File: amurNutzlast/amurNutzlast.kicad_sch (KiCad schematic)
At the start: 6 parts, among them J1 Conn_01x08, J3 Conn_01x02, J4 Conn_01x08, J5 Conn_01x07, J7 Conn_01x07, J8 Conn_01x20

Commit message: layout ftdi placement
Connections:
- net GND: no longer J3.1 (Pin_1)
- net fpga/FTDI_CTS: now also J7.4 (Pin_4); no longer J7.7 (Pin_7)
- net fpga/FTDI_DCD: now also J7.1 (Pin_1); no longer J7.4 (Pin_4)
- net fpga/FTDI_DSR: now also J7.2 (Pin_2); no longer J7.5 (Pin_5)
- net fpga/FTDI_DTR: now also J7.3 (Pin_3); no longer J7.6 (Pin_6)
- net fpga/FTDI_RTS: now also J7.5 (Pin_5); no longer J7.1 (Pin_1)
- net fpga/FTDI_RX: now also J7.7 (Pin_7); no longer J7.3 (Pin_3)
- net fpga/FTDI_TX: now also J7.6 (Pin_6); no longer J7.2 (Pin_2)
- new net +5V: J3.1 (Pin_1)
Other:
- note added: "jumper to supply input power to the FPGA"
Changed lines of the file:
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@@
   (junction (at 144.78 68.58) (diameter 0) (color 0 0 0 0)
   )
+  (wire (pts (xy 111.76 160.02) (xy 137.16 160.02))
+    (stroke (width 0) (type default))
+  )
   (wire (pts (xy 154.94 139.7) (xy 132.08 139.7))
     (stroke (width 0) (type default))
   )
+  (wire (pts (xy 68.58 20.32) (xy 68.58 27.94))
+    (stroke (width 0) (type default))
+  )
   (wire (pts (xy 129.54 137.16) (xy 154.94 137.16))
     (stroke (width 0) (type default))
   )
+  (wire (pts (xy 111.76 157.48) (xy 134.62 157.48))
+    (stroke (width 0) (type default))
+  )
   (wire (pts (xy 129.54 152.4) (xy 129.54 137.16))
     (stroke (width 0) (type default))
@@
     (stroke (width 0) (type default))
   )
+  (wire (pts (xy 111.76 152.4) (xy 129.54 152.4))
+    (stroke (width 0) (type default))
+  )
   (wire (pts (xy 111.76 132.08) (xy 114.3 132.08))
     (stroke (width 0) (type default))
@@
     (stroke (width 0) (type default))
   )
-  (wire (pts (xy 132.08 154.94) (xy 111.76 154.94))
+  (wire (pts (xy 111.76 162.56) (xy 139.7 162.56))
     (stroke (width 0) (type default))
   )
@@
     (stroke (width 0) (type default))
   )
+  (wire (pts (xy 185.42 68.58) (xy 200.66 68.58))
+    (stroke (width 0) (type default))
+  )
+  (wire (pts (xy 55.88 27.94) (xy 68.58 27.94))
+    (stroke (width 0) (type default))
+  )
+  (wire (pts (xy 111.76 96.52) (xy 114.3 96.52))
+    (stroke (width 0) (type default))
+  )
+  (wire (pts (xy 147.32 81.28) (xy 152.4 81.28))
+    (stroke (width 0) (type default))
+  )
+  (wire (pts (xy 111.76 63.5) (xy 139.7 63.5))
+    (stroke (width 0) (type default))
+  )
+  (wire (pts (xy 111.76 129.54) (xy 114.3 129.54))
+    (stroke (width 0) (type default))
+  )
+  (wire (pts (xy 144.78 167.64) (xy 144.78 152.4))
+    (stroke (width 0) (type default))
+  )
+  (wire (pts (xy 111.76 121.92) (xy 114.3 121.92))
+    (stroke (width 0) (type default))
+  )
+  (wire (pts (xy 185.42 137.16) (xy 200.66 137.16))
+    (stroke (width 0) (type default))
+  )
+  (wire (pts (xy 111.76 109.22) (xy 114.3 109.22))
+    (stroke (width 0) (type default))
+  )
+  (wire (pts (xy 185.42 66.04) (xy 200.66 66.04))
+    (stroke (width 0) (type default))
+  )
+  (wire (pts (xy 111.76 124.46) (xy 114.3 124.46))
+    (stroke (width 0) (type default))
+  )
+  (wire (pts (xy 154.94 76.2) (xy 154.94 81.28))
+    (stroke (width 0) (type default))
+  )
+  (wire (pts (xy 149.86 33.02) (xy 149.86 71.12))
+    (stroke (width 0) (type default))
+  )
+  (wire (pts (xy 185.42 73.66) (xy 193.04 73.66))
+    (stroke (width 0) (type default))
+  )
+  (wire (pts (xy 111.76 111.76) (xy 114.3 111.76))
+    (stroke (width 0) (type default))
+  )
+  (wire (pts (xy 154.94 149.86) (xy 142.24 149.86))
+    (stroke (width 0) (type default))
+  )
+  (wire (pts (xy 111.76 71.12) (xy 149.86 71.12))
+    (stroke (width 0) (type default))
+  )
+  (wire (pts (xy 111.76 60.96) (xy 157.48 60.96))
+    (stroke (width 0) (type default))
+  )
+  (wire (pts (xy 111.76 101.6) (xy 114.3 101.6))
+    (stroke (width 0) (type default))
+  )
   (wire (pts (xy 111.76 167.64) (xy 144.78 167.64))
     (stroke (width 0) (type default))
   )
-  (wire (pts (xy 185.42 68.58) (xy 200.66 68.58))
-    (stroke (width 0) (type default))
-  )
-  (wire (pts (xy 60.96 27.94) (xy 55.88 27.94))
-    (stroke (width 0) (type default))
-  )
-  (wire (pts (xy 111.76 96.52) (xy 114.3 96.52))
-    (stroke (width 0) (type default))
-  )
-  (wire (pts (xy 147.32 81.28) (xy 152.4 81.28))
-    (stroke (width 0) (type default))
-  )
-  (wire (pts (xy 111.76 63.5) (xy 139.7 63.5))
-    (stroke (width 0) (type default))
-  )
-  (wire (pts (xy 111.76 129.54) (xy 114.3 129.54))
-    (stroke (width 0) (type default))
-  )
-  (wire (pts (xy 111.76 152.4) (xy 129.54 152.4))
-    (stroke (width 0) (type default))
-  )
-  (wire (pts (xy 144.78 167.64) (xy 144.78 152.4))
-    (stroke (width 0) (type default))
-  )
-  (wire (pts (xy 111.76 162.56) (xy 139.7 162.56))
-    (stroke (width 0) (type default))
-  )
-  (wire (pts (xy 111.76 121.92) (xy 114.3 121.92))
-    (stroke (width 0) (type default))
-  )
-  (wire (pts (xy 185.42 137.16) (xy 200.66 137.16))
-    (stroke (width 0) (type default))
-  )
-  (wire (pts (xy 111.76 109.22) (xy 114.3 109.22))
-    (stroke (width 0) (type default))
-  )
-  (wire (pts (xy 185.42 66.04) (xy 200.66 66.04))
-    (stroke (width 0) (type default))
-  )
-  (wire (pts (xy 111.76 124.46) (xy 114.3 124.46))
-    (stroke (width 0) (type default))
-  )
-  (wire (pts (xy 154.94 76.2) (xy 154.94 81.28))
-    (stroke (width 0) (type default))
-  )
-  (wire (pts (xy 149.86 33.02) (xy 149.86 71.12))
-    (stroke (width 0) (type default))
-  )
-  (wire (pts (xy 185.42 73.66) (xy 193.04 73.66))
-    (stroke (width 0) (type default))
-  )
-  (wire (pts (xy 111.76 111.76) (xy 114.3 111.76))
-    (stroke (width 0) (type default))
-  )
-  (wire (pts (xy 154.94 149.86) (xy 142.24 149.86))
-    (stroke (width 0) (type default))
-  )
-  (wire (pts (xy 111.76 71.12) (xy 149.86 71.12))
-    (stroke (width 0) (type default))
-  )
-  (wire (pts (xy 111.76 60.96) (xy 157.48 60.96))
-    (stroke (width 0) (type default))
-  )
-  (wire (pts (xy 111.76 101.6) (xy 114.3 101.6))
-    (stroke (width 0) (type default))
-  )
   (wire (pts (xy 147.32 78.74) (xy 147.32 81.28))
     (stroke (width 0) (type default))
@@
     (stroke (width 0) (type default))
   )
-  (wire (pts (xy 137.16 160.02) (xy 111.76 160.02))
-    (stroke (width 0) (type default))
-  )
   (wire (pts (xy 111.76 68.58) (xy 144.78 68.58))
     (stroke (width 0) (type default))
@@
     (stroke (width 0) (type default))
   )
-  (wire (pts (xy 111.76 157.48) (xy 134.62 157.48))
-    (stroke (width 0) (type default))
-  )
   (wire (pts (xy 185.42 71.12) (xy 200.66 71.12))
     (stroke (width 0) (type default))
@@
     (stroke (width 0) (type default))
   )
-  (wire (pts (xy 142.24 165.1) (xy 111.76 165.1))
+  (wire (pts (xy 111.76 165.1) (xy 142.24 165.1))
     (stroke (width 0) (type default))
   )
@@
     (stroke (width 0) (type default))
   )
-  (wire (pts (xy 60.96 27.94) (xy 60.96 35.56))
-    (stroke (width 0) (type default))
-  )
   (wire (pts (xy 137.16 144.78) (xy 137.16 160.02))
     (stroke (width 0) (type default))
   )
+  (wire (pts (xy 111.76 154.94) (xy 132.08 154.94))
+    (stroke (width 0) (type default))
+  )
   (wire (pts (xy 111.76 58.42) (xy 157.48 58.42))
     (stroke (width 0) (type default))
@@
   (wire (pts (xy 152.4 81.28) (xy 152.4 73.66))
     (stroke (width 0) (type default))
+  )
+  (text "jumper to supply input\npower to the FPGA" (at 73.66 22.86 0)
+    (effects (font (size 1.27 1.27)) (justify left bottom))
   )
   (label "ICE_CDONE" (at 116.84 60.96 0) (fields_autoplaced)
@@
     )
   )
-  (symbol (lib_id "power:GND") (at 60.96 35.56 0) (unit 1)
-    (in_bom yes) (on_board yes) (dnp no) (fields_autoplaced)
-    (property "Reference" "#PWR087" (at 60.96 41.91 0)
-      (effects (font (size 1.27 1.27)) hide)
-    )
-    (property "Value" "GND" (at 60.96 40.64 0)
-      (effects (font (size 1.27 1.27)))
-    )
-    (property "Footprint" "" (at 60.96 35.56 0)
-      (effects (font (size 1.27 1.27)) hide)
-    )
-    (property "Datasheet" "" (at 60.96 35.56 0)
+  (symbol (lib_id "power:+5V") (at 68.58 20.32 0) (unit 1)
+    (in_bom yes) (on_board yes) (dnp no) (fields_autoplaced)
+    (property "Reference" "#PWR087" (at 68.58 24.13 0)
+      (effects (font (size 1.27 1.27)) hide)
+    )
+    (property "Value" "+5V" (at 68.58 15.24 0)
+      (effects (font (size 1.27 1.27)))
+    )
+    (property "Footprint" "" (at 68.58 20.32 0)
+      (effects (font (size 1.27 1.27)) hide)
+    )
+    (property "Datasheet" "" (at 68.58 20.32 0)
       (effects (font (size 1.27 1.27)) hide)
     )
@@
       (effects (font (size 1.27 1.27)) (justify right))
     )
-    (pin "FTDI_RTS" input (at 111.76 152.4 0)
-      (effects (font (size 1.27 1.27)) (justify right))
-    )
-    (pin "FTDI_TX" input (at 111.76 154.94 0)
-      (effects (font (size 1.27 1.27)) (justify right))
-    )
-    (pin "FTDI_DCD" input (at 111.76 160.02 0)
-      (effects (font (size 1.27 1.27)) (justify right))
-    )
-    (pin "FTDI_DSR" input (at 111.76 162.56 0)
-      (effects (font (size 1.27 1.27)) (justify right))
-    )
-    (pin "FTDI_DTR" input (at 111.76 165.1 0)
-      (effects (font (size 1.27 1.27)) (justify right))
-    )
-    (pin "FTDI_CTS" input (at 111.76 167.64 0)
-      (effects (font (size 1.27 1.27)) (justify right))
-    )
-    (pin "FTDI_RX" output (at 111.76 157.48 0)
-      (effects (font (size 1.27 1.27)) (justify right))
-    )
+    (pin "FTDI_RTS" input (at 111.76 162.56 0)
+      (effects (font (size 1.27 1.27)) (justify right))
+    )
+    (pin "FTDI_TX" input (at 111.76 165.1 0)
+      (effects (font (size 1.27 1.27)) (justify right))
+    )
+    (pin "FTDI_DCD" input (at 111.76 152.4 0)
+      (effects (font (size 1.27 1.27)) (justify right))
+    )
+    (pin "FTDI_DSR" input (at 111.76 154.94 0)
+      (effects (font (size 1.27 1.27)) (justify right))
+    )
+    (pin "FTDI_DTR" input (at 111.76 157.48 0)
+      (effects (font (size 1.27 1.27)) (justify right))
+    )
+    (pin "FTDI_CTS" input (at 111.76 160.02 0)
+      (effects (font (size 1.27 1.27)) (justify right))
+    )
+    (pin "FTDI_RX" output (at 111.76 167.64 0)
+      (effects (font (size 1.27 1.27)) (justify right))
+    )

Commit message: ftdi layout continuation
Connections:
- net ftdi/CTS: now also J5.4 (Pin_4); no longer J5.1 (Pin_1)
- net ftdi/DCD: now also J5.1 (Pin_1); no longer J5.4 (Pin_4)
- net ftdi/DSR: now also J5.2 (Pin_2); no longer J5.3 (Pin_3)
- net ftdi/DTR: now also J5.3 (Pin_3); no longer J5.2 (Pin_2)
- net ftdi/RTS: now also J5.5 (Pin_5); no longer J5.7 (Pin_7)
- net ftdi/RX: now also J5.7 (Pin_7); no longer J5.5 (Pin_5)

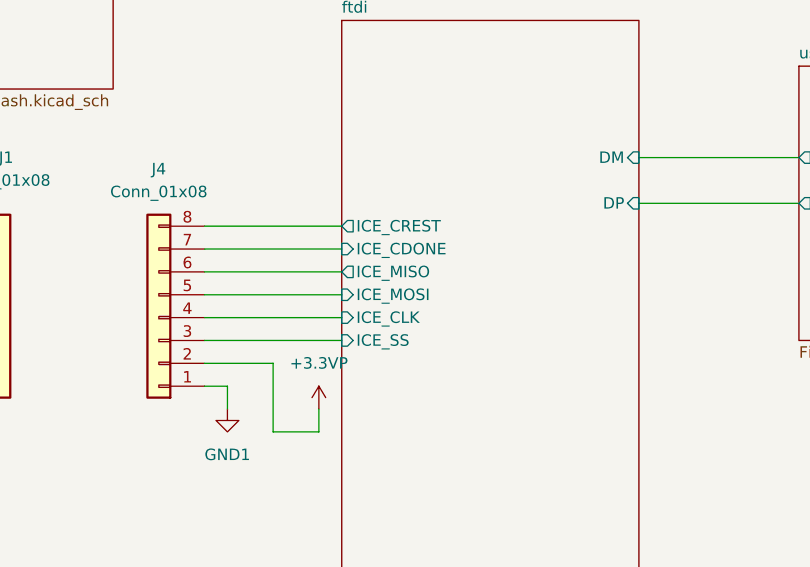
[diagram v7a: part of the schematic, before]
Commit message: ftdi layout finish
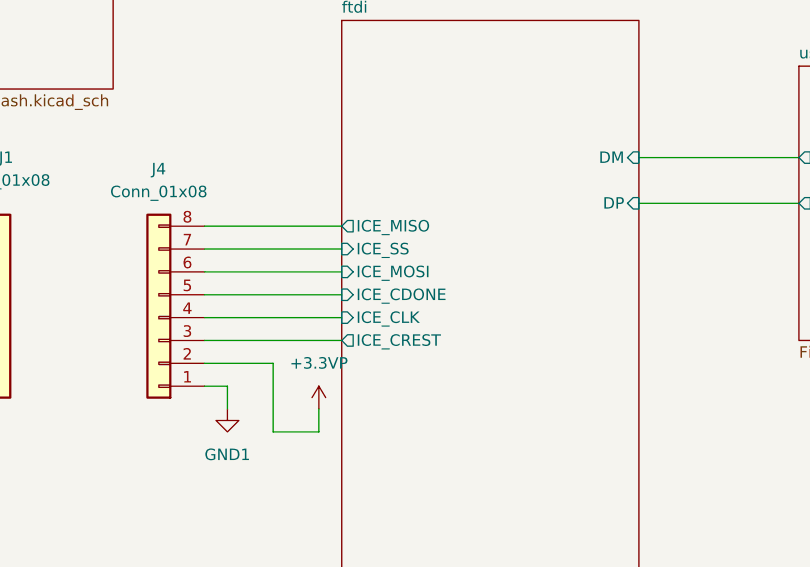
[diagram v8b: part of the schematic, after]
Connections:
- net ftdi/ICE_CDONE: now also J4.5 (Pin_5); no longer J4.7 (Pin_7)
- net ftdi/ICE_CREST: now also J4.3 (Pin_3); no longer J4.8 (Pin_8)
- net ftdi/ICE_MISO: now also J4.8 (Pin_8); no longer J4.6 (Pin_6)
- net ftdi/ICE_MOSI: now also J4.6 (Pin_6); no longer J4.5 (Pin_5)
- net ftdi/ICE_SS: now also J4.7 (Pin_7); no longer J4.3 (Pin_3)
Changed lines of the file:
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@@
+    (stroke (width 0) (type default))
+  )
+  (wire (pts (xy 185.42 58.42) (xy 200.66 58.42))
     (stroke (width 0) (type default))
   )
@@
     (stroke (width 0) (type default))
   )
+  (wire (pts (xy 185.42 63.5) (xy 200.66 63.5))
+    (stroke (width 0) (type default))
+  )
   (wire (pts (xy 111.76 121.92) (xy 114.3 121.92))
     (stroke (width 0) (type default))
@@
     (stroke (width 0) (type default))
   )
+  (wire (pts (xy 111.76 124.46) (xy 114.3 124.46))
+    (stroke (width 0) (type default))
+  )
   (wire (pts (xy 185.42 66.04) (xy 200.66 66.04))
     (stroke (width 0) (type default))
   )
-  (wire (pts (xy 111.76 124.46) (xy 114.3 124.46))
-    (stroke (width 0) (type default))
-  )
   (wire (pts (xy 154.94 76.2) (xy 154.94 81.28))
     (stroke (width 0) (type default))
@@
     (stroke (width 0) (type default))
   )
-  (wire (pts (xy 185.42 63.5) (xy 200.66 63.5))
-    (stroke (width 0) (type default))
-  )
   (wire (pts (xy 60.96 20.32) (xy 60.96 25.4))
     (stroke (width 0) (type default))
@@
     (stroke (width 0) (type default))
   )
+  (wire (pts (xy 185.42 60.96) (xy 200.66 60.96))
+    (stroke (width 0) (type default))
+  )
   (wire (pts (xy 53.34 86.36) (xy 71.12 86.36))
     (stroke (width 0) (type default))
@@
     (stroke (width 0) (type default))
   )
-  (wire (pts (xy 185.42 60.96) (xy 200.66 60.96))
-    (stroke (width 0) (type default))
-  )
   (wire (pts (xy 139.7 147.32) (xy 154.94 147.32))
     (stroke (width 0) (type default))
   )
+  (wire (pts (xy 111.76 142.24) (xy 114.3 142.24))
+    (stroke (width 0) (type default))
+  )
   (wire (pts (xy 185.42 71.12) (xy 200.66 71.12))
     (stroke (width 0) (type default))
   )
-  (wire (pts (xy 111.76 142.24) (xy 114.3 142.24))
-    (stroke (width 0) (type default))
-  )
   (wire (pts (xy 111.76 134.62) (xy 114.3 134.62))
     (stroke (width 0) (type default))
@@
   )
   (wire (pts (xy 154.94 144.78) (xy 137.16 144.78))
-    (stroke (width 0) (type default))
-  )
-  (wire (pts (xy 185.42 58.42) (xy 200.66 58.42))
     (stroke (width 0) (type default))
   )
@@
       (effects (font (size 1.27 1.27)) (justify left))
     )
-    (pin "ICE_MISO" output (at 200.66 63.5 180)
-      (effects (font (size 1.27 1.27)) (justify left))
-    )
-    (pin "ICE_CDONE" input (at 200.66 60.96 180)
-      (effects (font (size 1.27 1.27)) (justify left))
-    )
-    (pin "ICE_MOSI" input (at 200.66 66.04 180)
-      (effects (font (size 1.27 1.27)) (justify left))
-    )
-    (pin "ICE_SS" input (at 200.66 71.12 180)
+    (pin "ICE_MISO" output (at 200.66 58.42 180)
+      (effects (font (size 1.27 1.27)) (justify left))
+    )
+    (pin "ICE_CDONE" input (at 200.66 66.04 180)
+      (effects (font (size 1.27 1.27)) (justify left))
+    )
+    (pin "ICE_MOSI" input (at 200.66 63.5 180)
+      (effects (font (size 1.27 1.27)) (justify left))
+    )
+    (pin "ICE_SS" input (at 200.66 60.96 180)
       (effects (font (size 1.27 1.27)) (justify left))
     )
@@
       (effects (font (size 1.27 1.27)) (justify left))
     )
-    (pin "ICE_CREST" output (at 200.66 58.42 180)
-      (effects (font (size 1.27 1.27)) (justify left))
-    )
+    (pin "ICE_CREST" output (at 200.66 71.12 180)
+      (effects (font (size 1.27 1.27)) (justify left))
+    )
